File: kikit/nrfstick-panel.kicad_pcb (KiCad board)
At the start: 4 copper layers, 78 x 103.5 mm, 681 parts, among them J1 USB_A, J2 programming conn, J3 IO00, J4 Reset, J6 UART2, SW1 SKRPABE010, U3 APX803L20-27SR-7, U4 CP2102C-Axx-xQFN24, U5 BM15C, Y1 32.768kHz

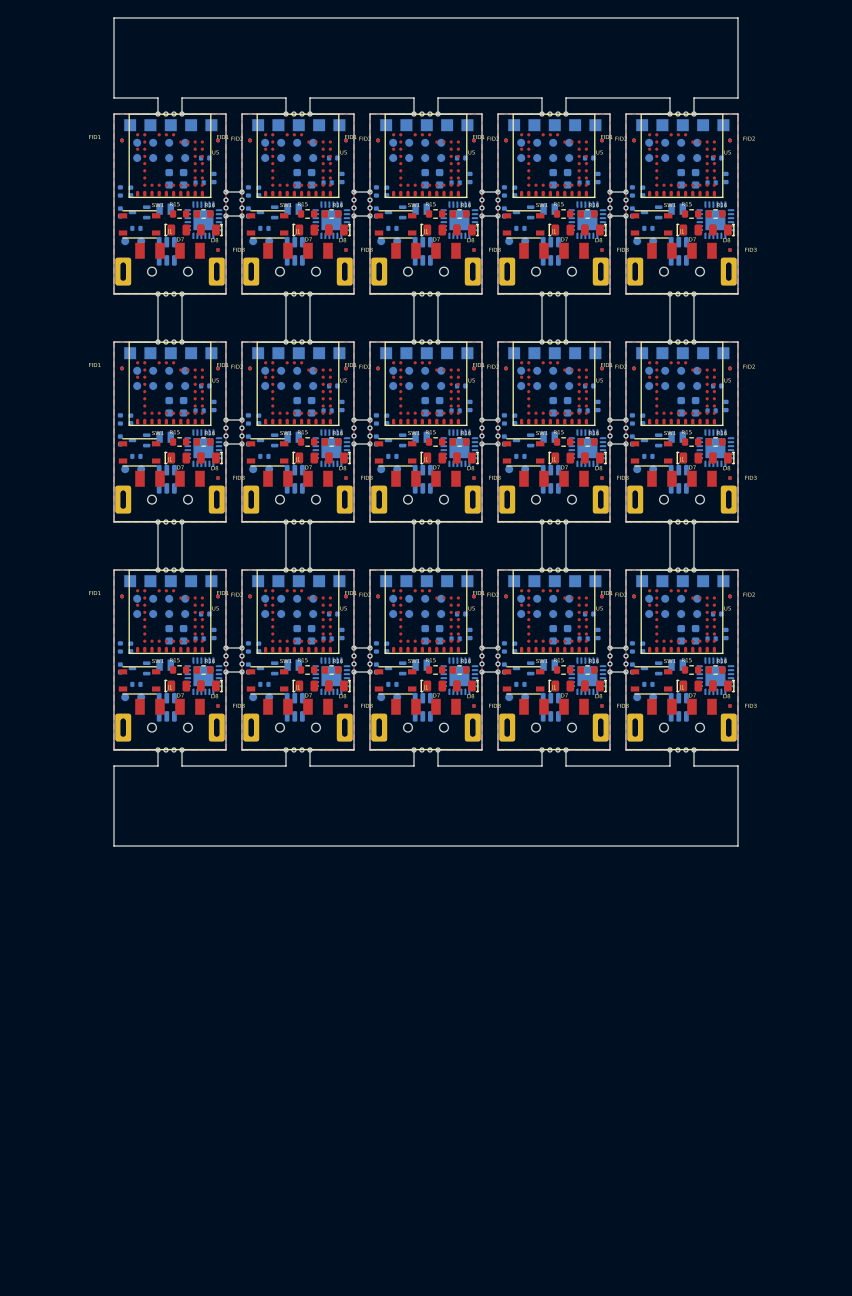
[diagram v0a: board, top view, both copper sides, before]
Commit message: panelize, new usb connector
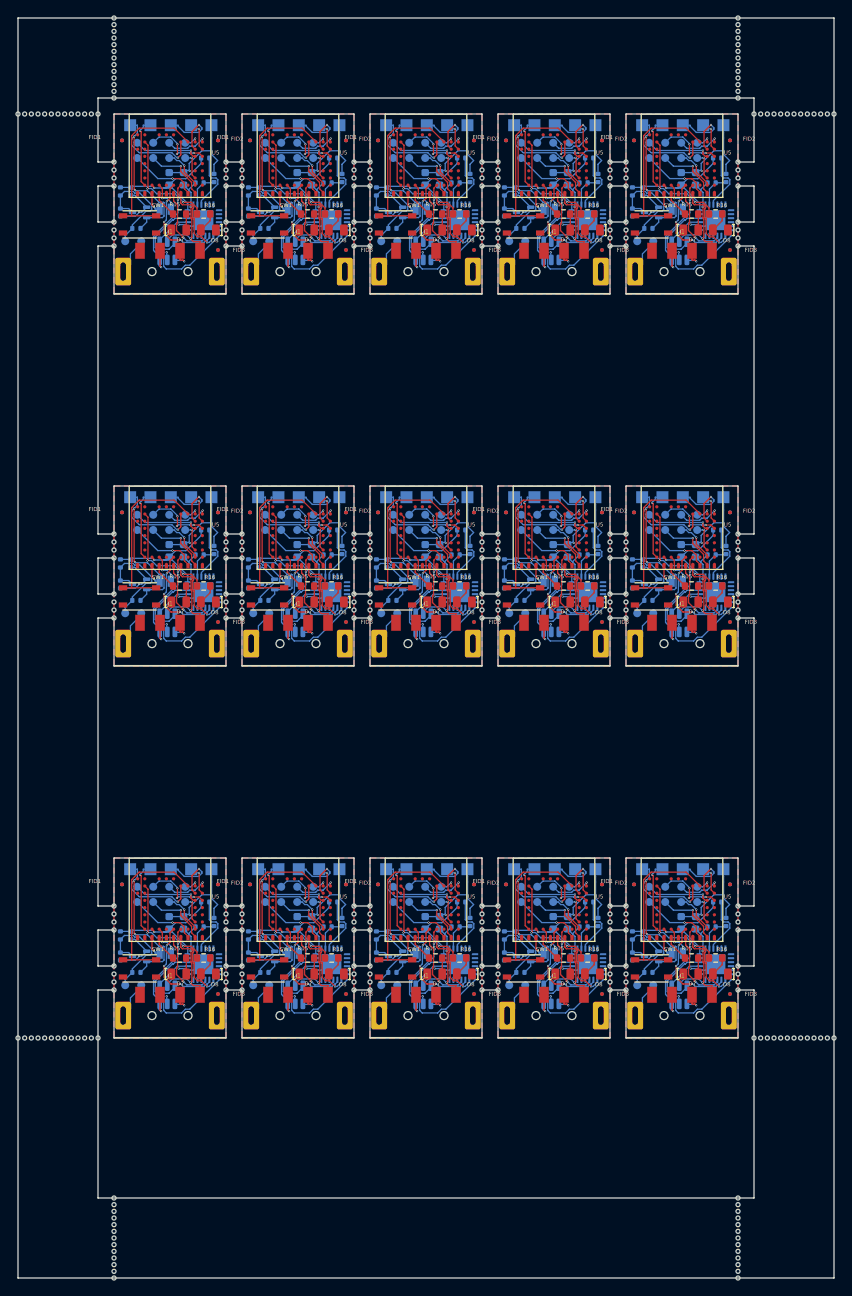
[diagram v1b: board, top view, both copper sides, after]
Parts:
- removed the C16 at (150.8, 70.2)
- removed the C16 at (134.8, 70.2)
- removed the C16 at (166.8, 70.2)
- removed the C16 at (150.8, 98.7)
- removed the C16 at (102.8, 70.2)
- removed the C16 at (134.8, 98.7)
- removed the C16 at (166.8, 98.7)
- removed the C16 at (102.8, 98.7)
- removed the C16 at (118.8, 98.7)
- removed the C16 at (118.8, 70.2)
- removed the C20 at (133.5, 101.3)
- removed the C20 at (133.5, 72.8)
- removed the C20 at (149.5, 72.8)
- removed the C20 at (101.5, 101.3)
- removed the C20 at (149.5, 101.3)
- removed the C20 at (101.5, 72.8)
- removed the C20 at (117.5, 72.8)
- removed the C20 at (165.5, 72.8)
- removed the C20 at (165.5, 101.3)
- removed the C20 at (117.5, 101.3)
- removed the C7 at (171.6, 97.1)
- removed the C7 at (139.6, 97.1)
- removed the C7 at (107.6, 97.1)
- removed the C7 at (171.6, 68.6)
- removed the C7 at (123.6, 97.1)
- removed the C7 at (155.6, 68.6)
- removed the C7 at (155.6, 97.1)
- removed the C7 at (139.6, 68.6)
- removed the C7 at (123.6, 68.6)
- removed the C7 at (107.6, 68.6)
- removed the C8 at (173.4, 97.1)
- removed the C8 at (125.4, 97.1)
- removed the C8 at (109.4, 68.6)
- removed the C8 at (173.4, 68.6)
- removed the C8 at (125.4, 68.6)
- removed the C8 at (157.4, 68.6)
- removed the C8 at (141.4, 68.6)
- removed the C8 at (141.4, 97.1)
- removed the C8 at (157.4, 97.1)
- removed the C8 at (109.4, 97.1)
- removed the D7 at (124.8, 103.5)
- removed the D7 at (140.8, 75.0)
- removed the D7 at (172.8, 103.5)
- removed the D7 at (172.8, 75.0)
- removed the D7 at (140.8, 103.5)
- removed the D7 at (108.8, 75.0)
- removed the D7 at (108.8, 103.5)
- removed the D7 at (156.8, 103.5)
- removed the D7 at (124.8, 75.0)
- removed the D7 at (156.8, 75.0)
- removed the D8 at (160.5, 103.5)
- removed the D8 at (176.5, 75.0)
- removed the D8 at (160.5, 75.0)
- removed the D8 at (144.5, 75.0)
- removed the D8 at (176.5, 103.5)
- removed the D8 at (112.5, 75.0)
- removed the D8 at (128.5, 103.5)
- removed the D8 at (144.5, 103.5)
- removed the D8 at (128.5, 75.0)
- removed the D8 at (112.5, 103.5)
- removed the FID1 at (101.7, 92.3)
- removed the FID1 at (165.7, 63.8)
- removed the FID1 at (149.7, 63.8)
- removed the FID1 at (133.7, 63.8)
- removed the FID1 at (117.7, 63.8)
- removed the FID1 at (117.7, 92.3)
- removed the FID1 at (165.7, 92.3)
- removed the FID1 at (101.7, 63.8)
- removed the FID1 at (149.7, 92.3)
- removed the FID1 at (133.7, 92.3)
- removed the FID2 at (145.7, 63.8)
- removed the FID2 at (161.7, 63.8)
- removed the FID2 at (177.7, 63.8)
- removed the FID2 at (113.7, 92.3)
- removed the FID2 at (145.7, 92.3)
- removed the FID2 at (177.7, 92.3)
- removed the FID2 at (129.7, 63.8)
- removed the FID2 at (129.7, 92.3)
- removed the FID2 at (161.7, 92.3)
- removed the FID2 at (113.7, 63.8)
- removed the FID3 at (113.7, 77.5)
- removed the FID3 at (129.7, 106.0)
- removed the FID3 at (113.7, 106.0)
- removed the FID3 at (129.7, 77.5)
- removed the FID3 at (177.7, 106.0)
- removed the FID3 at (177.7, 77.5)
- removed the FID3 at (161.7, 77.5)
- removed the FID3 at (161.7, 106.0)
- removed the FID3 at (145.7, 77.5)
- removed the FID3 at (145.7, 106.0)
- removed the FID4 at (133.7, 63.8)
- removed the FID4 at (165.7, 92.3)
- removed the FID4 at (149.7, 92.3)
- removed the FID4 at (133.7, 92.3)
- removed the FID4 at (149.7, 63.8)
- removed the FID4 at (101.7, 63.8)
- removed the FID4 at (101.7, 92.3)
- removed the FID4 at (117.7, 63.8)
- removed the FID4 at (117.7, 92.3)
- removed the FID4 at (165.7, 63.8)
- removed the FID5 at (129.7, 92.3)
- removed the FID5 at (177.7, 63.8)
- removed the FID5 at (145.7, 92.3)
- removed the FID5 at (161.7, 63.8)
- removed the FID5 at (177.7, 92.3)
- removed the FID5 at (145.7, 63.8)
- removed the FID5 at (129.7, 63.8)
- removed the FID5 at (113.7, 63.8)
- removed the FID5 at (161.7, 92.3)
- removed the FID5 at (113.7, 92.3)
- removed the FID6 at (145.7, 77.5)
- removed the FID6 at (161.7, 77.5)
- removed the FID6 at (145.7, 106.0)
- removed the FID6 at (177.7, 106.0)
- removed the FID6 at (113.7, 106.0)
- removed the FID6 at (177.7, 77.5)
- removed the FID6 at (129.7, 77.5)
- removed the FID6 at (113.7, 77.5)
- removed the FID6 at (161.7, 106.0)
- removed the FID6 at (129.7, 106.0)
- removed the H2 at (175.1, 106.3)
- removed the H2 at (127.1, 77.8)
- removed the H2 at (159.1, 106.3)
- removed the H2 at (175.1, 77.8)
- removed the H2 at (143.1, 77.8)
- removed the H2 at (111.1, 77.8)
- removed the H2 at (111.1, 106.3)
- removed the H2 at (159.1, 77.8)
- removed the H2 at (143.1, 106.3)
- removed the H2 at (127.1, 106.3)
- removed the J1 at (123.7, 108.7)
- removed the J1 at (155.7, 80.2)
- removed the J1 at (171.7, 80.2)
- removed the J1 at (107.7, 80.2)
- removed the J1 at (155.7, 108.7)
- removed the J1 at (139.7, 80.2)
- removed the J1 at (107.7, 108.7)
- removed the J1 at (171.7, 108.7)
- removed the J1 at (123.7, 80.2)
- removed the J1 at (139.7, 108.7)
- removed the J2 at (171.8, 61.9)
- removed the J2 at (123.8, 90.4)
- removed the J2 at (155.8, 61.9)
- removed the J2 at (107.8, 90.4)
- removed the J2 at (107.8, 61.9)
- removed the J2 at (139.8, 61.9)
- removed the J2 at (171.8, 90.4)
- removed the J2 at (123.8, 61.9)
- removed the J2 at (139.8, 90.4)
- removed the J2 at (155.8, 90.4)
- removed the J3 at (106.6, 64.1)
- removed the J3 at (154.6, 64.1)
- removed the J3 at (122.6, 92.6)
- removed the J3 at (170.6, 64.1)
- removed the J3 at (154.6, 92.6)
- removed the J3 at (106.6, 92.6)
- removed the J3 at (138.6, 64.1)
- removed the J3 at (170.6, 92.6)
- removed the J3 at (138.6, 92.6)
- removed the J3 at (122.6, 64.1)
- removed the J4 at (151.1, 104.9)
- removed the J4 at (135.1, 76.4)
- removed the J4 at (167.1, 76.4)
- removed the J4 at (151.1, 76.4)
- removed the J4 at (103.1, 104.9)
- removed the J4 at (167.1, 104.9)
- removed the J4 at (119.1, 104.9)
- removed the J4 at (103.1, 76.4)
- removed the J4 at (119.1, 76.4)
- removed the J4 at (135.1, 104.9)
- removed the J6 at (122.6, 66.0)
- removed the J6 at (138.6, 66.0)
- removed the J6 at (106.6, 66.0)
- removed the J6 at (170.6, 66.0)
- removed the J6 at (154.6, 66.0)
- removed the J6 at (138.6, 94.5)
- removed the J6 at (170.6, 94.5)
- removed the J6 at (106.6, 94.5)
- removed the J6 at (122.6, 94.5)
- removed the J6 at (154.6, 94.5)
- removed the R15 at (108.9, 101.5)
- removed the R15 at (172.9, 101.5)
- removed the R15 at (124.9, 101.5)
- removed the R15 at (156.9, 101.5)
- removed the R15 at (172.9, 73.0)
- removed the R15 at (156.9, 73.0)
- removed the R15 at (140.9, 73.0)
- removed the R15 at (140.9, 101.5)
- removed the R15 at (124.9, 73.0)
- removed the R15 at (108.9, 73.0)
- removed the R16 at (143.9, 101.5)
- removed the R16 at (127.9, 73.0)
- removed the R16 at (175.9, 73.0)
- removed the R16 at (159.9, 73.0)
- removed the R16 at (159.9, 101.5)
- removed the R16 at (127.9, 101.5)
- removed the R16 at (111.9, 101.5)
- removed the R16 at (111.9, 73.0)
- removed the R16 at (175.9, 101.5)
- removed the R16 at (143.9, 73.0)
- removed the R17 at (135.5, 103.3)
- removed the R17 at (103.5, 103.3)
- removed the R17 at (167.5, 103.3)
- removed the R17 at (151.5, 103.3)
- removed the R17 at (119.5, 103.3)
- removed the R17 at (151.5, 74.8)
- removed the R17 at (119.5, 74.8)
- removed the R17 at (103.5, 74.8)
- removed the R17 at (135.5, 74.8)
- removed the R17 at (167.5, 74.8)
- removed the R29 at (101.5, 70.2)
- removed the R29 at (165.5, 98.7)
- removed the R29 at (165.5, 70.2)
- removed the R29 at (149.5, 70.2)
- removed the R29 at (149.5, 98.7)
- removed the R29 at (133.5, 70.2)
- removed the R29 at (133.5, 98.7)
- removed the R29 at (117.5, 98.7)
- removed the R29 at (117.5, 70.2)
- removed the R29 at (101.5, 98.7)
- removed the R7 at (176.1, 66.0)
- removed the R7 at (144.1, 66.0)
- removed the R7 at (128.1, 94.5)
- removed the R7 at (112.1, 94.5)
- removed the R7 at (160.1, 94.5)
- removed the R7 at (112.1, 66.0)
- removed the R7 at (144.1, 94.5)
- removed the R7 at (160.1, 66.0)
- removed the R7 at (128.1, 66.0)
- removed the R7 at (176.1, 94.5)
- removed the R8 at (175.4, 97.6)
- removed the R8 at (175.4, 69.1)
- removed the R8 at (159.4, 69.1)
- removed the R8 at (111.4, 69.1)
- removed the R8 at (143.4, 69.1)
- removed the R8 at (143.4, 97.6)
- removed the R8 at (111.4, 97.6)
- removed the R8 at (127.4, 69.1)
- removed the R8 at (159.4, 97.6)
- removed the R8 at (127.4, 97.6)
- removed the R9 at (129.2, 97.0)
- removed the R9 at (161.2, 97.0)
- removed the R9 at (113.2, 97.0)
- removed the R9 at (177.2, 97.0)
- removed the R9 at (177.2, 68.5)
- removed the R9 at (161.2, 68.5)
- removed the R9 at (113.2, 68.5)
- removed the R9 at (145.2, 97.0)
- removed the R9 at (129.2, 68.5)
- removed the R9 at (145.2, 68.5)
- removed the SW1 at (151.9, 74.3)
- removed the SW1 at (167.9, 102.8)
- removed the SW1 at (135.9, 74.3)
- removed the SW1 at (103.9, 102.8)
- removed the SW1 at (103.9, 74.3)
- removed the SW1 at (119.9, 102.8)
- removed the SW1 at (167.9, 74.3)
- removed the SW1 at (135.9, 102.8)
- removed the SW1 at (119.9, 74.3)
- removed the SW1 at (151.9, 102.8)
- removed the U3 at (103.9, 72.8)
- removed the U3 at (151.9, 101.3)
- removed the U3 at (119.9, 101.3)
- removed the U3 at (119.9, 72.8)
- removed the U3 at (103.9, 101.3)
- removed the U3 at (151.9, 72.8)
- removed the U3 at (167.9, 72.8)
- removed the U3 at (167.9, 101.3)
- removed the U3 at (135.9, 101.3)
- removed the U3 at (135.9, 72.8)
- removed the U4 at (175.9, 73.8)
- removed the U4 at (127.9, 102.3)
- removed the U4 at (143.9, 102.3)
- removed the U4 at (175.9, 102.3)
- removed the U4 at (159.9, 73.8)
- removed the U4 at (127.9, 73.8)
- removed the U4 at (111.9, 73.8)
- removed the U4 at (111.9, 102.3)
- removed the U4 at (143.9, 73.8)
- removed the U4 at (159.9, 102.3)
- removed the U5 at (155.7, 91.4)
- removed the U5 at (123.7, 91.4)
- removed the U5 at (139.7, 91.4)
- removed the U5 at (155.7, 62.9)
- removed the U5 at (107.7, 91.4)
- removed the U5 at (171.7, 62.9)
- removed the U5 at (171.7, 91.4)
- removed the U5 at (107.7, 62.9)
- removed the U5 at (123.7, 62.9)
- removed the U5 at (139.7, 62.9)
- removed the Y1 at (155.1, 72.4)
- removed the Y1 at (107.1, 72.4)
- removed the Y1 at (139.1, 72.4)
- removed the Y1 at (155.1, 100.9)
- removed the Y1 at (139.1, 100.9)
- removed the Y1 at (123.1, 100.9)
- removed the Y1 at (107.1, 100.9)
- removed the Y1 at (171.1, 72.4)
- removed the Y1 at (123.1, 72.4)
- removed the Y1 at (171.1, 100.9)
- removed the Z1 at (155.3, 106.2)
- removed the Z1 at (107.3, 77.7)
- removed the Z1 at (139.3, 49.2)
- removed the Z1 at (139.3, 106.2)
- removed the Z1 at (123.3, 77.7)
- removed the Z1 at (123.3, 106.2)
- removed the Z1 at (139.3, 77.7)
- removed the Z1 at (155.3, 77.7)
- removed the Z1 at (171.3, 49.2)
- removed the Z1 at (155.3, 49.2)
- removed the Z1 at (171.3, 77.7)
- removed the Z1 at (107.3, 106.2)
- removed the Z1 at (123.3, 49.2)
- removed the Z1 at (171.3, 106.2)
- removed the Z1 at (107.3, 49.2)
- added C16: 0.10uF/50v, Capacitor_SMD:C_0402_1005Metric, B.Cu at (166.8, 88.2)
- added C16: 0.10uF/50v, Capacitor_SMD:C_0402_1005Metric, B.Cu at (102.8, 134.7)
- added C16: 0.10uF/50v, Capacitor_SMD:C_0402_1005Metric, B.Cu at (134.8, 88.2)
- added C16: 0.10uF/50v, Capacitor_SMD:C_0402_1005Metric, B.Cu at (102.8, 88.2)
- added C16: 0.10uF/50v, Capacitor_SMD:C_0402_1005Metric, B.Cu at (150.8, 134.7)
- added C16: 0.10uF/50v, Capacitor_SMD:C_0402_1005Metric, B.Cu at (118.8, 88.2)
- added C16: 0.10uF/50v, Capacitor_SMD:C_0402_1005Metric, B.Cu at (118.8, 134.7)
- added C16: 0.10uF/50v, Capacitor_SMD:C_0402_1005Metric, B.Cu at (134.8, 134.7)
- added C16: 0.10uF/50v, Capacitor_SMD:C_0402_1005Metric, B.Cu at (150.8, 88.2)
- added C16: 0.10uF/50v, Capacitor_SMD:C_0402_1005Metric, B.Cu at (166.8, 134.7)
- added C20: 0.10uF/50v, Capacitor_SMD:C_0402_1005Metric, B.Cu at (117.5, 137.3)
- added C20: 0.10uF/50v, Capacitor_SMD:C_0402_1005Metric, B.Cu at (133.5, 90.8)
- added C20: 0.10uF/50v, Capacitor_SMD:C_0402_1005Metric, B.Cu at (165.5, 90.8)
- added C20: 0.10uF/50v, Capacitor_SMD:C_0402_1005Metric, B.Cu at (101.5, 90.8)
- added C20: 0.10uF/50v, Capacitor_SMD:C_0402_1005Metric, B.Cu at (149.5, 90.8)
- added C20: 0.10uF/50v, Capacitor_SMD:C_0402_1005Metric, B.Cu at (117.5, 90.8)
- added C20: 0.10uF/50v, Capacitor_SMD:C_0402_1005Metric, B.Cu at (101.5, 137.3)
- added C20: 0.10uF/50v, Capacitor_SMD:C_0402_1005Metric, B.Cu at (149.5, 137.3)
- added C20: 0.10uF/50v, Capacitor_SMD:C_0402_1005Metric, B.Cu at (133.5, 137.3)
- added C20: 0.10uF/50v, Capacitor_SMD:C_0402_1005Metric, B.Cu at (165.5, 137.3)
- added C7: 4.7uF/10V, Capacitor_SMD:C_0603_1608Metric, B.Cu at (155.6, 133.1)
- added C7: 4.7uF/10V, Capacitor_SMD:C_0603_1608Metric, B.Cu at (139.6, 133.1)
- added C7: 4.7uF/10V, Capacitor_SMD:C_0603_1608Metric, B.Cu at (107.6, 86.6)
- added C7: 4.7uF/10V, Capacitor_SMD:C_0603_1608Metric, B.Cu at (171.6, 133.1)
- added C7: 4.7uF/10V, Capacitor_SMD:C_0603_1608Metric, B.Cu at (155.6, 86.6)
- added C7: 4.7uF/10V, Capacitor_SMD:C_0603_1608Metric, B.Cu at (171.6, 86.6)
- added C7: 4.7uF/10V, Capacitor_SMD:C_0603_1608Metric, B.Cu at (123.6, 86.6)
- added C7: 4.7uF/10V, Capacitor_SMD:C_0603_1608Metric, B.Cu at (107.6, 133.1)
- added C7: 4.7uF/10V, Capacitor_SMD:C_0603_1608Metric, B.Cu at (139.6, 86.6)
- added C7: 4.7uF/10V, Capacitor_SMD:C_0603_1608Metric, B.Cu at (123.6, 133.1)
- added C8: 4.7uF/10V, Capacitor_SMD:C_0603_1608Metric, B.Cu at (173.4, 86.6)
- added C8: 4.7uF/10V, Capacitor_SMD:C_0603_1608Metric, B.Cu at (141.4, 133.1)
- added C8: 4.7uF/10V, Capacitor_SMD:C_0603_1608Metric, B.Cu at (109.4, 86.6)
- added C8: 4.7uF/10V, Capacitor_SMD:C_0603_1608Metric, B.Cu at (157.4, 133.1)
- added C8: 4.7uF/10V, Capacitor_SMD:C_0603_1608Metric, B.Cu at (125.4, 133.1)
- added C8: 4.7uF/10V, Capacitor_SMD:C_0603_1608Metric, B.Cu at (109.4, 133.1)
- added C8: 4.7uF/10V, Capacitor_SMD:C_0603_1608Metric, B.Cu at (141.4, 86.6)
- added C8: 4.7uF/10V, Capacitor_SMD:C_0603_1608Metric, B.Cu at (125.4, 86.6)
- added C8: 4.7uF/10V, Capacitor_SMD:C_0603_1608Metric, B.Cu at (157.4, 86.6)
- added C8: 4.7uF/10V, Capacitor_SMD:C_0603_1608Metric, B.Cu at (173.4, 133.1)
- added D7: BLUE LED, footprint:LED_0805_2012Metric, F.Cu at (124.8, 93.0)
- added D7: BLUE LED, footprint:LED_0805_2012Metric, F.Cu at (156.8, 139.5)
- added D7: BLUE LED, footprint:LED_0805_2012Metric, F.Cu at (172.8, 93.0)
- added D7: BLUE LED, footprint:LED_0805_2012Metric, F.Cu at (140.8, 93.0)
- added D7: BLUE LED, footprint:LED_0805_2012Metric, F.Cu at (140.8, 139.5)
- added D7: BLUE LED, footprint:LED_0805_2012Metric, F.Cu at (124.8, 139.5)
- added D7: BLUE LED, footprint:LED_0805_2012Metric, F.Cu at (108.8, 139.5)
- added D7: BLUE LED, footprint:LED_0805_2012Metric, F.Cu at (156.8, 93.0)
- added D7: BLUE LED, footprint:LED_0805_2012Metric, F.Cu at (172.8, 139.5)
- added D7: BLUE LED, footprint:LED_0805_2012Metric, F.Cu at (108.8, 93.0)
- added D8: RED LED, footprint:LED_0805_2012Metric, F.Cu at (112.5, 93.0)
- added D8: RED LED, footprint:LED_0805_2012Metric, F.Cu at (112.5, 139.5)
- added D8: RED LED, footprint:LED_0805_2012Metric, F.Cu at (128.5, 139.5)
- added D8: RED LED, footprint:LED_0805_2012Metric, F.Cu at (160.5, 139.5)
- added D8: RED LED, footprint:LED_0805_2012Metric, F.Cu at (176.5, 93.0)
- added D8: RED LED, footprint:LED_0805_2012Metric, F.Cu at (128.5, 93.0)
- added D8: RED LED, footprint:LED_0805_2012Metric, F.Cu at (176.5, 139.5)
- added D8: RED LED, footprint:LED_0805_2012Metric, F.Cu at (160.5, 93.0)
- added D8: RED LED, footprint:LED_0805_2012Metric, F.Cu at (144.5, 139.5)
- added D8: RED LED, footprint:LED_0805_2012Metric, F.Cu at (144.5, 93.0)
- added FID1: Fiducial, Fiducial:Fiducial_0.5mm_Mask1mm, F.Cu at (133.7, 128.3)
- added FID1: Fiducial, Fiducial:Fiducial_0.5mm_Mask1mm, F.Cu at (133.7, 81.8)
- added FID1: Fiducial, Fiducial:Fiducial_0.5mm_Mask1mm, F.Cu at (117.7, 128.3)
- added FID1: Fiducial, Fiducial:Fiducial_0.5mm_Mask1mm, F.Cu at (165.7, 128.3)
- added FID1: Fiducial, Fiducial:Fiducial_0.5mm_Mask1mm, F.Cu at (149.7, 128.3)
- added FID1: Fiducial, Fiducial:Fiducial_0.5mm_Mask1mm, F.Cu at (101.7, 81.8)
- added FID1: Fiducial, Fiducial:Fiducial_0.5mm_Mask1mm, F.Cu at (165.7, 81.8)
- added FID1: Fiducial, Fiducial:Fiducial_0.5mm_Mask1mm, F.Cu at (149.7, 81.8)
- added FID1: Fiducial, Fiducial:Fiducial_0.5mm_Mask1mm, F.Cu at (117.7, 81.8)
- added FID1: Fiducial, Fiducial:Fiducial_0.5mm_Mask1mm, F.Cu at (101.7, 128.3)
- added FID2: Fiducial, Fiducial:Fiducial_0.5mm_Mask1mm, F.Cu at (145.7, 81.8)
- added FID2: Fiducial, Fiducial:Fiducial_0.5mm_Mask1mm, F.Cu at (177.7, 81.8)
- added FID2: Fiducial, Fiducial:Fiducial_0.5mm_Mask1mm, F.Cu at (177.7, 128.3)
- added FID2: Fiducial, Fiducial:Fiducial_0.5mm_Mask1mm, F.Cu at (161.7, 81.8)
- added FID2: Fiducial, Fiducial:Fiducial_0.5mm_Mask1mm, F.Cu at (129.7, 81.8)
- added FID2: Fiducial, Fiducial:Fiducial_0.5mm_Mask1mm, F.Cu at (145.7, 128.3)
- added FID2: Fiducial, Fiducial:Fiducial_0.5mm_Mask1mm, F.Cu at (113.7, 81.8)
- added FID2: Fiducial, Fiducial:Fiducial_0.5mm_Mask1mm, F.Cu at (129.7, 128.3)
- added FID2: Fiducial, Fiducial:Fiducial_0.5mm_Mask1mm, F.Cu at (113.7, 128.3)
- added FID2: Fiducial, Fiducial:Fiducial_0.5mm_Mask1mm, F.Cu at (161.7, 128.3)
- added FID3: Fiducial, Fiducial:Fiducial_0.5mm_Mask1mm, F.Cu at (161.7, 95.5)
- added FID3: Fiducial, Fiducial:Fiducial_0.5mm_Mask1mm, F.Cu at (129.7, 142.0)
- added FID3: Fiducial, Fiducial:Fiducial_0.5mm_Mask1mm, F.Cu at (145.7, 142.0)
- added FID3: Fiducial, Fiducial:Fiducial_0.5mm_Mask1mm, F.Cu at (113.7, 142.0)
- added FID3: Fiducial, Fiducial:Fiducial_0.5mm_Mask1mm, F.Cu at (145.7, 95.5)
- added FID3: Fiducial, Fiducial:Fiducial_0.5mm_Mask1mm, F.Cu at (161.7, 142.0)
- added FID3: Fiducial, Fiducial:Fiducial_0.5mm_Mask1mm, F.Cu at (113.7, 95.5)
- added FID3: Fiducial, Fiducial:Fiducial_0.5mm_Mask1mm, F.Cu at (177.7, 142.0)
- added FID3: Fiducial, Fiducial:Fiducial_0.5mm_Mask1mm, F.Cu at (129.7, 95.5)
- added FID3: Fiducial, Fiducial:Fiducial_0.5mm_Mask1mm, F.Cu at (177.7, 95.5)
- added FID4: Fiducial, Fiducial:Fiducial_0.5mm_Mask1mm, B.Cu at (117.7, 128.3)
- added FID4: Fiducial, Fiducial:Fiducial_0.5mm_Mask1mm, B.Cu at (101.7, 128.3)
- added FID4: Fiducial, Fiducial:Fiducial_0.5mm_Mask1mm, B.Cu at (133.7, 128.3)
- added FID4: Fiducial, Fiducial:Fiducial_0.5mm_Mask1mm, B.Cu at (117.7, 81.8)
- added FID4: Fiducial, Fiducial:Fiducial_0.5mm_Mask1mm, B.Cu at (101.7, 81.8)
- added FID4: Fiducial, Fiducial:Fiducial_0.5mm_Mask1mm, B.Cu at (165.7, 128.3)
- added FID4: Fiducial, Fiducial:Fiducial_0.5mm_Mask1mm, B.Cu at (149.7, 128.3)
- added FID4: Fiducial, Fiducial:Fiducial_0.5mm_Mask1mm, B.Cu at (165.7, 81.8)
- added FID4: Fiducial, Fiducial:Fiducial_0.5mm_Mask1mm, B.Cu at (133.7, 81.8)
- added FID4: Fiducial, Fiducial:Fiducial_0.5mm_Mask1mm, B.Cu at (149.7, 81.8)
- added FID5: Fiducial, Fiducial:Fiducial_0.5mm_Mask1mm, B.Cu at (177.7, 128.3)
- added FID5: Fiducial, Fiducial:Fiducial_0.5mm_Mask1mm, B.Cu at (177.7, 81.8)
- added FID5: Fiducial, Fiducial:Fiducial_0.5mm_Mask1mm, B.Cu at (161.7, 128.3)
- added FID5: Fiducial, Fiducial:Fiducial_0.5mm_Mask1mm, B.Cu at (129.7, 81.8)
- added FID5: Fiducial, Fiducial:Fiducial_0.5mm_Mask1mm, B.Cu at (113.7, 128.3)
- added FID5: Fiducial, Fiducial:Fiducial_0.5mm_Mask1mm, B.Cu at (145.7, 81.8)
- added FID5: Fiducial, Fiducial:Fiducial_0.5mm_Mask1mm, B.Cu at (145.7, 128.3)
- added FID5: Fiducial, Fiducial:Fiducial_0.5mm_Mask1mm, B.Cu at (113.7, 81.8)
- added FID5: Fiducial, Fiducial:Fiducial_0.5mm_Mask1mm, B.Cu at (129.7, 128.3)
- added FID5: Fiducial, Fiducial:Fiducial_0.5mm_Mask1mm, B.Cu at (161.7, 81.8)
- added FID6: Fiducial, Fiducial:Fiducial_0.5mm_Mask1mm, B.Cu at (177.7, 142.0)
- added FID6: Fiducial, Fiducial:Fiducial_0.5mm_Mask1mm, B.Cu at (145.7, 95.5)
- added FID6: Fiducial, Fiducial:Fiducial_0.5mm_Mask1mm, B.Cu at (129.7, 95.5)
- added FID6: Fiducial, Fiducial:Fiducial_0.5mm_Mask1mm, B.Cu at (129.7, 142.0)
- added FID6: Fiducial, Fiducial:Fiducial_0.5mm_Mask1mm, B.Cu at (161.7, 142.0)
- added FID6: Fiducial, Fiducial:Fiducial_0.5mm_Mask1mm, B.Cu at (161.7, 95.5)
- added FID6: Fiducial, Fiducial:Fiducial_0.5mm_Mask1mm, B.Cu at (113.7, 142.0)
- added FID6: Fiducial, Fiducial:Fiducial_0.5mm_Mask1mm, B.Cu at (145.7, 142.0)
- added FID6: Fiducial, Fiducial:Fiducial_0.5mm_Mask1mm, B.Cu at (177.7, 95.5)
- added FID6: Fiducial, Fiducial:Fiducial_0.5mm_Mask1mm, B.Cu at (113.7, 95.5)
- added H2: Shepherd, footprint:shepherd-neg, B.Cu at (143.1, 95.8)
- added H2: Shepherd, footprint:shepherd-neg, B.Cu at (127.1, 142.3)
- added H2: Shepherd, footprint:shepherd-neg, B.Cu at (175.1, 142.3)
- added H2: Shepherd, footprint:shepherd-neg, B.Cu at (159.1, 142.3)
- added H2: Shepherd, footprint:shepherd-neg, B.Cu at (143.1, 142.3)
- added H2: Shepherd, footprint:shepherd-neg, B.Cu at (111.1, 95.8)
- added H2: Shepherd, footprint:shepherd-neg, B.Cu at (127.1, 95.8)
- added H2: Shepherd, footprint:shepherd-neg, B.Cu at (111.1, 142.3)
- added H2: Shepherd, footprint:shepherd-neg, B.Cu at (175.1, 95.8)
- added H2: Shepherd, footprint:shepherd-neg, B.Cu at (159.1, 95.8)
- added J1: USB_A, footprint:connector-USB-A-male-smd-Molex-480372100, F.Cu at (155.7, 144.7)
- added J1: USB_A, footprint:connector-USB-A-male-smd-Molex-480372100, F.Cu at (123.7, 98.2)
- added J1: USB_A, footprint:connector-USB-A-male-smd-Molex-480372100, F.Cu at (107.7, 144.7)
- added J1: USB_A, footprint:connector-USB-A-male-smd-Molex-480372100, F.Cu at (171.7, 98.2)
- added J1: USB_A, footprint:connector-USB-A-male-smd-Molex-480372100, F.Cu at (171.7, 144.7)
- added J1: USB_A, footprint:connector-USB-A-male-smd-Molex-480372100, F.Cu at (139.7, 98.2)
- added J1: USB_A, footprint:connector-USB-A-male-smd-Molex-480372100, F.Cu at (139.7, 144.7)
- added J1: USB_A, footprint:connector-USB-A-male-smd-Molex-480372100, F.Cu at (155.7, 98.2)
- added J1: USB_A, footprint:connector-USB-A-male-smd-Molex-480372100, F.Cu at (107.7, 98.2)
- added J1: USB_A, footprint:connector-USB-A-male-smd-Molex-480372100, F.Cu at (123.7, 144.7)
- added J2: programming conn, footprint:program-nrf, B.Cu at (107.8, 79.9)
- added J2: programming conn, footprint:program-nrf, B.Cu at (171.8, 79.9)
- added J2: programming conn, footprint:program-nrf, B.Cu at (123.8, 126.4)
- added J2: programming conn, footprint:program-nrf, B.Cu at (171.8, 126.4)
- added J2: programming conn, footprint:program-nrf, B.Cu at (139.8, 79.9)
- added J2: programming conn, footprint:program-nrf, B.Cu at (155.8, 126.4)
- added J2: programming conn, footprint:program-nrf, B.Cu at (107.8, 126.4)
- added J2: programming conn, footprint:program-nrf, B.Cu at (123.8, 79.9)
- added J2: programming conn, footprint:program-nrf, B.Cu at (155.8, 79.9)
- added J2: programming conn, footprint:program-nrf, B.Cu at (139.8, 126.4)
- added J3: IO00, footprint:Conn_Pads_1x04_P2.00mm_D1.00mm, B.Cu at (170.6, 82.1)
- added J3: IO00, footprint:Conn_Pads_1x04_P2.00mm_D1.00mm, B.Cu at (106.6, 82.1)
- added J3: IO00, footprint:Conn_Pads_1x04_P2.00mm_D1.00mm, B.Cu at (154.6, 82.1)
- added J3: IO00, footprint:Conn_Pads_1x04_P2.00mm_D1.00mm, B.Cu at (154.6, 128.6)
- added J3: IO00, footprint:Conn_Pads_1x04_P2.00mm_D1.00mm, B.Cu at (122.6, 82.1)
- added J3: IO00, footprint:Conn_Pads_1x04_P2.00mm_D1.00mm, B.Cu at (170.6, 128.6)
- added J3: IO00, footprint:Conn_Pads_1x04_P2.00mm_D1.00mm, B.Cu at (106.6, 128.6)
- added J3: IO00, footprint:Conn_Pads_1x04_P2.00mm_D1.00mm, B.Cu at (138.6, 128.6)
- added J3: IO00, footprint:Conn_Pads_1x04_P2.00mm_D1.00mm, B.Cu at (122.6, 128.6)
- added J3: IO00, footprint:Conn_Pads_1x04_P2.00mm_D1.00mm, B.Cu at (138.6, 82.1)
- added J4: Reset, footprint:Conn_Pads_2x01_P2.00mm_D1.00mm, B.Cu at (103.1, 140.9)
- added J4: Reset, footprint:Conn_Pads_2x01_P2.00mm_D1.00mm, B.Cu at (103.1, 94.4)
- added J4: Reset, footprint:Conn_Pads_2x01_P2.00mm_D1.00mm, B.Cu at (135.1, 94.4)
- added J4: Reset, footprint:Conn_Pads_2x01_P2.00mm_D1.00mm, B.Cu at (151.1, 140.9)
- added J4: Reset, footprint:Conn_Pads_2x01_P2.00mm_D1.00mm, B.Cu at (167.1, 94.4)
- added J4: Reset, footprint:Conn_Pads_2x01_P2.00mm_D1.00mm, B.Cu at (119.1, 140.9)
- added J4: Reset, footprint:Conn_Pads_2x01_P2.00mm_D1.00mm, B.Cu at (135.1, 140.9)
- added J4: Reset, footprint:Conn_Pads_2x01_P2.00mm_D1.00mm, B.Cu at (119.1, 94.4)
- added J4: Reset, footprint:Conn_Pads_2x01_P2.00mm_D1.00mm, B.Cu at (167.1, 140.9)
- added J4: Reset, footprint:Conn_Pads_2x01_P2.00mm_D1.00mm, B.Cu at (151.1, 94.4)
- added J6: UART2, footprint:Conn_Pads_1x04_P2.00mm_D1.00mm, B.Cu at (170.6, 84.0)
- added J6: UART2, footprint:Conn_Pads_1x04_P2.00mm_D1.00mm, B.Cu at (138.6, 130.5)
- added J6: UART2, footprint:Conn_Pads_1x04_P2.00mm_D1.00mm, B.Cu at (122.6, 130.5)
- added J6: UART2, footprint:Conn_Pads_1x04_P2.00mm_D1.00mm, B.Cu at (106.6, 84.0)
- added J6: UART2, footprint:Conn_Pads_1x04_P2.00mm_D1.00mm, B.Cu at (154.6, 84.0)
- added J6: UART2, footprint:Conn_Pads_1x04_P2.00mm_D1.00mm, B.Cu at (154.6, 130.5)
- added J6: UART2, footprint:Conn_Pads_1x04_P2.00mm_D1.00mm, B.Cu at (106.6, 130.5)
- added J6: UART2, footprint:Conn_Pads_1x04_P2.00mm_D1.00mm, B.Cu at (138.6, 84.0)
- added J6: UART2, footprint:Conn_Pads_1x04_P2.00mm_D1.00mm, B.Cu at (170.6, 130.5)
- added J6: UART2, footprint:Conn_Pads_1x04_P2.00mm_D1.00mm, B.Cu at (122.6, 84.0)
- added KiKit_MB_55_1: NPTH, NPTH, F.Cu at (162.7, 131.0)
- added KiKit_MB_55_2: NPTH, NPTH, F.Cu at (162.7, 132.0)
- added KiKit_MB_55_3: NPTH, NPTH, F.Cu at (162.7, 133.0)
- added KiKit_MB_55_4: NPTH, NPTH, F.Cu at (162.7, 134.0)
- added KiKit_MB_56_1: NPTH, NPTH, F.Cu at (162.7, 138.5)
- added KiKit_MB_56_2: NPTH, NPTH, F.Cu at (162.7, 139.5)
- added KiKit_MB_56_3: NPTH, NPTH, F.Cu at (162.7, 140.5)
- added KiKit_MB_56_4: NPTH, NPTH, F.Cu at (162.7, 141.5)
- added KiKit_MB_57_1: NPTH, NPTH, F.Cu at (164.7, 134.0)
- added KiKit_MB_57_2: NPTH, NPTH, F.Cu at (164.7, 133.0)
- added KiKit_MB_57_3: NPTH, NPTH, F.Cu at (164.7, 132.0)
- added KiKit_MB_57_4: NPTH, NPTH, F.Cu at (164.7, 131.0)
- added KiKit_MB_58_1: NPTH, NPTH, F.Cu at (164.7, 141.5)
- added KiKit_MB_58_2: NPTH, NPTH, F.Cu at (164.7, 140.5)
- added KiKit_MB_58_3: NPTH, NPTH, F.Cu at (164.7, 139.5)
- added KiKit_MB_58_4: NPTH, NPTH, F.Cu at (164.7, 138.5)
- added KiKit_MB_59_1: NPTH, NPTH, F.Cu at (178.7, 131.0)
- added KiKit_MB_59_2: NPTH, NPTH, F.Cu at (178.7, 132.0)
- added KiKit_MB_59_3: NPTH, NPTH, F.Cu at (178.7, 133.0)
- added KiKit_MB_59_4: NPTH, NPTH, F.Cu at (178.7, 134.0)
- added KiKit_MB_60_1: NPTH, NPTH, F.Cu at (178.7, 138.5)
- added KiKit_MB_60_2: NPTH, NPTH, F.Cu at (178.7, 139.5)
- added KiKit_MB_60_3: NPTH, NPTH, F.Cu at (178.7, 140.5)
- added KiKit_MB_60_4: NPTH, NPTH, F.Cu at (178.7, 141.5)
- added KiKit_MB_61_1: NPTH, NPTH, F.Cu at (100.7, 20.0)
- added KiKit_MB_61_10: NPTH, NPTH, F.Cu at (100.7, 27.5)
- added KiKit_MB_61_11: NPTH, NPTH, F.Cu at (100.7, 28.3)
- added KiKit_MB_61_12: NPTH, NPTH, F.Cu at (100.7, 29.2)
- added KiKit_MB_61_13: NPTH, NPTH, F.Cu at (100.7, 30.0)
- added KiKit_MB_61_2: NPTH, NPTH, F.Cu at (100.7, 20.8)
- added KiKit_MB_61_3: NPTH, NPTH, F.Cu at (100.7, 21.7)
- added KiKit_MB_61_4: NPTH, NPTH, F.Cu at (100.7, 22.5)
- added KiKit_MB_61_5: NPTH, NPTH, F.Cu at (100.7, 23.3)
- added KiKit_MB_61_6: NPTH, NPTH, F.Cu at (100.7, 24.2)
- added KiKit_MB_61_7: NPTH, NPTH, F.Cu at (100.7, 25.0)
- added KiKit_MB_61_8: NPTH, NPTH, F.Cu at (100.7, 25.8)
- added KiKit_MB_61_9: NPTH, NPTH, F.Cu at (100.7, 26.7)
- added KiKit_MB_62_1: NPTH, NPTH, F.Cu at (178.7, 20.0)
- added KiKit_MB_62_10: NPTH, NPTH, F.Cu at (178.7, 27.5)
- added KiKit_MB_62_11: NPTH, NPTH, F.Cu at (178.7, 28.3)
- added KiKit_MB_62_12: NPTH, NPTH, F.Cu at (178.7, 29.2)
- added KiKit_MB_62_13: NPTH, NPTH, F.Cu at (178.7, 30.0)
- added KiKit_MB_62_2: NPTH, NPTH, F.Cu at (178.7, 20.8)
- added KiKit_MB_62_3: NPTH, NPTH, F.Cu at (178.7, 21.7)
- added KiKit_MB_62_4: NPTH, NPTH, F.Cu at (178.7, 22.5)
- added KiKit_MB_62_5: NPTH, NPTH, F.Cu at (178.7, 23.3)
- added KiKit_MB_62_6: NPTH, NPTH, F.Cu at (178.7, 24.2)
- added KiKit_MB_62_7: NPTH, NPTH, F.Cu at (178.7, 25.0)
- added KiKit_MB_62_8: NPTH, NPTH, F.Cu at (178.7, 25.8)
- added KiKit_MB_62_9: NPTH, NPTH, F.Cu at (178.7, 26.7)
- added KiKit_MB_63_1: NPTH, NPTH, F.Cu at (100.7, 167.5)
- added KiKit_MB_63_10: NPTH, NPTH, F.Cu at (100.7, 175.0)
- added KiKit_MB_63_11: NPTH, NPTH, F.Cu at (100.7, 175.8)
- added KiKit_MB_63_12: NPTH, NPTH, F.Cu at (100.7, 176.7)
- added KiKit_MB_63_13: NPTH, NPTH, F.Cu at (100.7, 177.5)
- added KiKit_MB_63_2: NPTH, NPTH, F.Cu at (100.7, 168.3)
- added KiKit_MB_63_3: NPTH, NPTH, F.Cu at (100.7, 169.2)
- added KiKit_MB_63_4: NPTH, NPTH, F.Cu at (100.7, 170.0)
- added KiKit_MB_63_5: NPTH, NPTH, F.Cu at (100.7, 170.8)
- added KiKit_MB_63_6: NPTH, NPTH, F.Cu at (100.7, 171.7)
- added KiKit_MB_63_7: NPTH, NPTH, F.Cu at (100.7, 172.5)
- added KiKit_MB_63_8: NPTH, NPTH, F.Cu at (100.7, 173.3)
- added KiKit_MB_63_9: NPTH, NPTH, F.Cu at (100.7, 174.2)
- added KiKit_MB_64_1: NPTH, NPTH, F.Cu at (178.7, 167.5)
- added KiKit_MB_64_10: NPTH, NPTH, F.Cu at (178.7, 175.0)
- added KiKit_MB_64_11: NPTH, NPTH, F.Cu at (178.7, 175.8)
- added KiKit_MB_64_12: NPTH, NPTH, F.Cu at (178.7, 176.7)
- added KiKit_MB_64_13: NPTH, NPTH, F.Cu at (178.7, 177.5)
- added KiKit_MB_64_2: NPTH, NPTH, F.Cu at (178.7, 168.3)
- added KiKit_MB_64_3: NPTH, NPTH, F.Cu at (178.7, 169.2)
- added KiKit_MB_64_4: NPTH, NPTH, F.Cu at (178.7, 170.0)
- added KiKit_MB_64_5: NPTH, NPTH, F.Cu at (178.7, 170.8)
- added KiKit_MB_64_6: NPTH, NPTH, F.Cu at (178.7, 171.7)
- added KiKit_MB_64_7: NPTH, NPTH, F.Cu at (178.7, 172.5)
- added KiKit_MB_64_8: NPTH, NPTH, F.Cu at (178.7, 173.3)
- added KiKit_MB_64_9: NPTH, NPTH, F.Cu at (178.7, 174.2)
- added KiKit_MB_65_1: NPTH, NPTH, F.Cu at (88.7, 32.0)
- added KiKit_MB_65_10: NPTH, NPTH, F.Cu at (96.2, 32.0)
- added KiKit_MB_65_11: NPTH, NPTH, F.Cu at (97.0, 32.0)
- added KiKit_MB_65_12: NPTH, NPTH, F.Cu at (97.9, 32.0)
- added KiKit_MB_65_13: NPTH, NPTH, F.Cu at (98.7, 32.0)
- added KiKit_MB_65_2: NPTH, NPTH, F.Cu at (89.5, 32.0)
- added KiKit_MB_65_3: NPTH, NPTH, F.Cu at (90.4, 32.0)
- added KiKit_MB_65_4: NPTH, NPTH, F.Cu at (91.2, 32.0)
- added KiKit_MB_65_5: NPTH, NPTH, F.Cu at (92.0, 32.0)
- added KiKit_MB_65_6: NPTH, NPTH, F.Cu at (92.9, 32.0)
- added KiKit_MB_65_7: NPTH, NPTH, F.Cu at (93.7, 32.0)
- added KiKit_MB_65_8: NPTH, NPTH, F.Cu at (94.5, 32.0)
- added KiKit_MB_65_9: NPTH, NPTH, F.Cu at (95.4, 32.0)
- added KiKit_MB_66_1: NPTH, NPTH, F.Cu at (180.7, 32.0)
- added KiKit_MB_66_10: NPTH, NPTH, F.Cu at (188.2, 32.0)
- added KiKit_MB_66_11: NPTH, NPTH, F.Cu at (189.0, 32.0)
- added KiKit_MB_66_12: NPTH, NPTH, F.Cu at (189.9, 32.0)
- added KiKit_MB_66_13: NPTH, NPTH, F.Cu at (190.7, 32.0)
- added KiKit_MB_66_2: NPTH, NPTH, F.Cu at (181.5, 32.0)
- added KiKit_MB_66_3: NPTH, NPTH, F.Cu at (182.4, 32.0)
- added KiKit_MB_66_4: NPTH, NPTH, F.Cu at (183.2, 32.0)
- added KiKit_MB_66_5: NPTH, NPTH, F.Cu at (184.0, 32.0)
- added KiKit_MB_66_6: NPTH, NPTH, F.Cu at (184.9, 32.0)
- added KiKit_MB_66_7: NPTH, NPTH, F.Cu at (185.7, 32.0)
- added KiKit_MB_66_8: NPTH, NPTH, F.Cu at (186.5, 32.0)
- added KiKit_MB_66_9: NPTH, NPTH, F.Cu at (187.4, 32.0)
- added KiKit_MB_67_1: NPTH, NPTH, F.Cu at (88.7, 147.5)
- added KiKit_MB_67_10: NPTH, NPTH, F.Cu at (96.2, 147.5)
- added KiKit_MB_67_11: NPTH, NPTH, F.Cu at (97.0, 147.5)
- added KiKit_MB_67_12: NPTH, NPTH, F.Cu at (97.9, 147.5)
- added KiKit_MB_67_13: NPTH, NPTH, F.Cu at (98.7, 147.5)
- added KiKit_MB_67_2: NPTH, NPTH, F.Cu at (89.5, 147.5)
- added KiKit_MB_67_3: NPTH, NPTH, F.Cu at (90.4, 147.5)
- added KiKit_MB_67_4: NPTH, NPTH, F.Cu at (91.2, 147.5)
- added KiKit_MB_67_5: NPTH, NPTH, F.Cu at (92.0, 147.5)
- added KiKit_MB_67_6: NPTH, NPTH, F.Cu at (92.9, 147.5)
- added KiKit_MB_67_7: NPTH, NPTH, F.Cu at (93.7, 147.5)
- added KiKit_MB_67_8: NPTH, NPTH, F.Cu at (94.5, 147.5)
- added KiKit_MB_67_9: NPTH, NPTH, F.Cu at (95.4, 147.5)
- added KiKit_MB_68_1: NPTH, NPTH, F.Cu at (180.7, 147.5)
- added KiKit_MB_68_10: NPTH, NPTH, F.Cu at (188.2, 147.5)
- added KiKit_MB_68_11: NPTH, NPTH, F.Cu at (189.0, 147.5)
- added KiKit_MB_68_12: NPTH, NPTH, F.Cu at (189.9, 147.5)
- added KiKit_MB_68_13: NPTH, NPTH, F.Cu at (190.7, 147.5)
- added KiKit_MB_68_2: NPTH, NPTH, F.Cu at (181.5, 147.5)
- added KiKit_MB_68_3: NPTH, NPTH, F.Cu at (182.4, 147.5)
- added KiKit_MB_68_4: NPTH, NPTH, F.Cu at (183.2, 147.5)
- added KiKit_MB_68_5: NPTH, NPTH, F.Cu at (184.0, 147.5)
- added KiKit_MB_68_6: NPTH, NPTH, F.Cu at (184.9, 147.5)
- added KiKit_MB_68_7: NPTH, NPTH, F.Cu at (185.7, 147.5)
- added KiKit_MB_68_8: NPTH, NPTH, F.Cu at (186.5, 147.5)
- added KiKit_MB_68_9: NPTH, NPTH, F.Cu at (187.4, 147.5)
- added R15: 47/0603/0.125W, Resistor_SMD:R_0603_1608Metric, F.Cu at (108.9, 137.5)
- added R15: 47/0603/0.125W, Resistor_SMD:R_0603_1608Metric, F.Cu at (156.9, 91.0)
- added R15: 47/0603/0.125W, Resistor_SMD:R_0603_1608Metric, F.Cu at (108.9, 91.0)
- added R15: 47/0603/0.125W, Resistor_SMD:R_0603_1608Metric, F.Cu at (124.9, 137.5)
- added R15: 47/0603/0.125W, Resistor_SMD:R_0603_1608Metric, F.Cu at (124.9, 91.0)
- added R15: 47/0603/0.125W, Resistor_SMD:R_0603_1608Metric, F.Cu at (140.9, 91.0)
- added R15: 47/0603/0.125W, Resistor_SMD:R_0603_1608Metric, F.Cu at (140.9, 137.5)
- added R15: 47/0603/0.125W, Resistor_SMD:R_0603_1608Metric, F.Cu at (156.9, 137.5)
- added R15: 47/0603/0.125W, Resistor_SMD:R_0603_1608Metric, F.Cu at (172.9, 91.0)
- added R15: 47/0603/0.125W, Resistor_SMD:R_0603_1608Metric, F.Cu at (172.9, 137.5)
- added R16: 270/0603/0.125W, Resistor_SMD:R_0603_1608Metric, F.Cu at (159.9, 137.5)
- added R16: 270/0603/0.125W, Resistor_SMD:R_0603_1608Metric, F.Cu at (175.9, 137.5)
- added R16: 270/0603/0.125W, Resistor_SMD:R_0603_1608Metric, F.Cu at (127.9, 137.5)
- added R16: 270/0603/0.125W, Resistor_SMD:R_0603_1608Metric, F.Cu at (127.9, 91.0)
- added R16: 270/0603/0.125W, Resistor_SMD:R_0603_1608Metric, F.Cu at (159.9, 91.0)
- added R16: 270/0603/0.125W, Resistor_SMD:R_0603_1608Metric, F.Cu at (143.9, 91.0)
- added R16: 270/0603/0.125W, Resistor_SMD:R_0603_1608Metric, F.Cu at (143.9, 137.5)
- added R16: 270/0603/0.125W, Resistor_SMD:R_0603_1608Metric, F.Cu at (111.9, 137.5)
- added R16: 270/0603/0.125W, Resistor_SMD:R_0603_1608Metric, F.Cu at (111.9, 91.0)
- added R16: 270/0603/0.125W, Resistor_SMD:R_0603_1608Metric, F.Cu at (175.9, 91.0)
- added R17: 100K, Resistor_SMD:R_0402_1005Metric, B.Cu at (103.5, 139.3)
- added R17: 100K, Resistor_SMD:R_0402_1005Metric, B.Cu at (135.5, 139.3)
- added R17: 100K, Resistor_SMD:R_0402_1005Metric, B.Cu at (135.5, 92.8)
- added R17: 100K, Resistor_SMD:R_0402_1005Metric, B.Cu at (151.5, 92.8)
- added R17: 100K, Resistor_SMD:R_0402_1005Metric, B.Cu at (103.5, 92.8)
- added R17: 100K, Resistor_SMD:R_0402_1005Metric, B.Cu at (119.5, 92.8)
- added R17: 100K, Resistor_SMD:R_0402_1005Metric, B.Cu at (167.5, 139.3)
- added R17: 100K, Resistor_SMD:R_0402_1005Metric, B.Cu at (119.5, 139.3)
- added R17: 100K, Resistor_SMD:R_0402_1005Metric, B.Cu at (167.5, 92.8)
- added R17: 100K, Resistor_SMD:R_0402_1005Metric, B.Cu at (151.5, 139.3)
- added R29: 1.00k, Resistor_SMD:R_0402_1005Metric, B.Cu at (117.5, 88.2)
- added R29: 1.00k, Resistor_SMD:R_0402_1005Metric, B.Cu at (149.5, 88.2)
- added R29: 1.00k, Resistor_SMD:R_0402_1005Metric, B.Cu at (117.5, 134.7)
- added R29: 1.00k, Resistor_SMD:R_0402_1005Metric, B.Cu at (133.5, 88.2)
- added R29: 1.00k, Resistor_SMD:R_0402_1005Metric, B.Cu at (165.5, 134.7)
- added R29: 1.00k, Resistor_SMD:R_0402_1005Metric, B.Cu at (101.5, 134.7)
- added R29: 1.00k, Resistor_SMD:R_0402_1005Metric, B.Cu at (165.5, 88.2)
- added R29: 1.00k, Resistor_SMD:R_0402_1005Metric, B.Cu at (101.5, 88.2)
- added R29: 1.00k, Resistor_SMD:R_0402_1005Metric, B.Cu at (149.5, 134.7)
- added R29: 1.00k, Resistor_SMD:R_0402_1005Metric, B.Cu at (133.5, 134.7)
- added R7: 1.00k, Resistor_SMD:R_0402_1005Metric, B.Cu at (112.1, 84.0)
- added R7: 1.00k, Resistor_SMD:R_0402_1005Metric, B.Cu at (128.1, 130.5)
- added R7: 1.00k, Resistor_SMD:R_0402_1005Metric, B.Cu at (176.1, 130.5)
- added R7: 1.00k, Resistor_SMD:R_0402_1005Metric, B.Cu at (144.1, 84.0)
- added R7: 1.00k, Resistor_SMD:R_0402_1005Metric, B.Cu at (160.1, 84.0)
- added R7: 1.00k, Resistor_SMD:R_0402_1005Metric, B.Cu at (160.1, 130.5)
- added R7: 1.00k, Resistor_SMD:R_0402_1005Metric, B.Cu at (144.1, 130.5)
- added R7: 1.00k, Resistor_SMD:R_0402_1005Metric, B.Cu at (112.1, 130.5)
- added R7: 1.00k, Resistor_SMD:R_0402_1005Metric, B.Cu at (176.1, 84.0)
- added R7: 1.00k, Resistor_SMD:R_0402_1005Metric, B.Cu at (128.1, 84.0)
- added R8: 22.1k, Resistor_SMD:R_0402_1005Metric, B.Cu at (127.4, 87.1)
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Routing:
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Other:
- board size 78 x 103.5 mm -> 102 x 157.5 mm
